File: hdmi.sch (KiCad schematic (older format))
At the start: 31 parts, among them J1901 Mini-HDMI, Q1901 NX3020NAKS, Q1902 NX3020NAKS, Q1903 NX3020NAKS, Q1904 NX3020NAKS, U1901 PCMF3HDMI2SZ, U1902 PCMF2HDMI2SZ

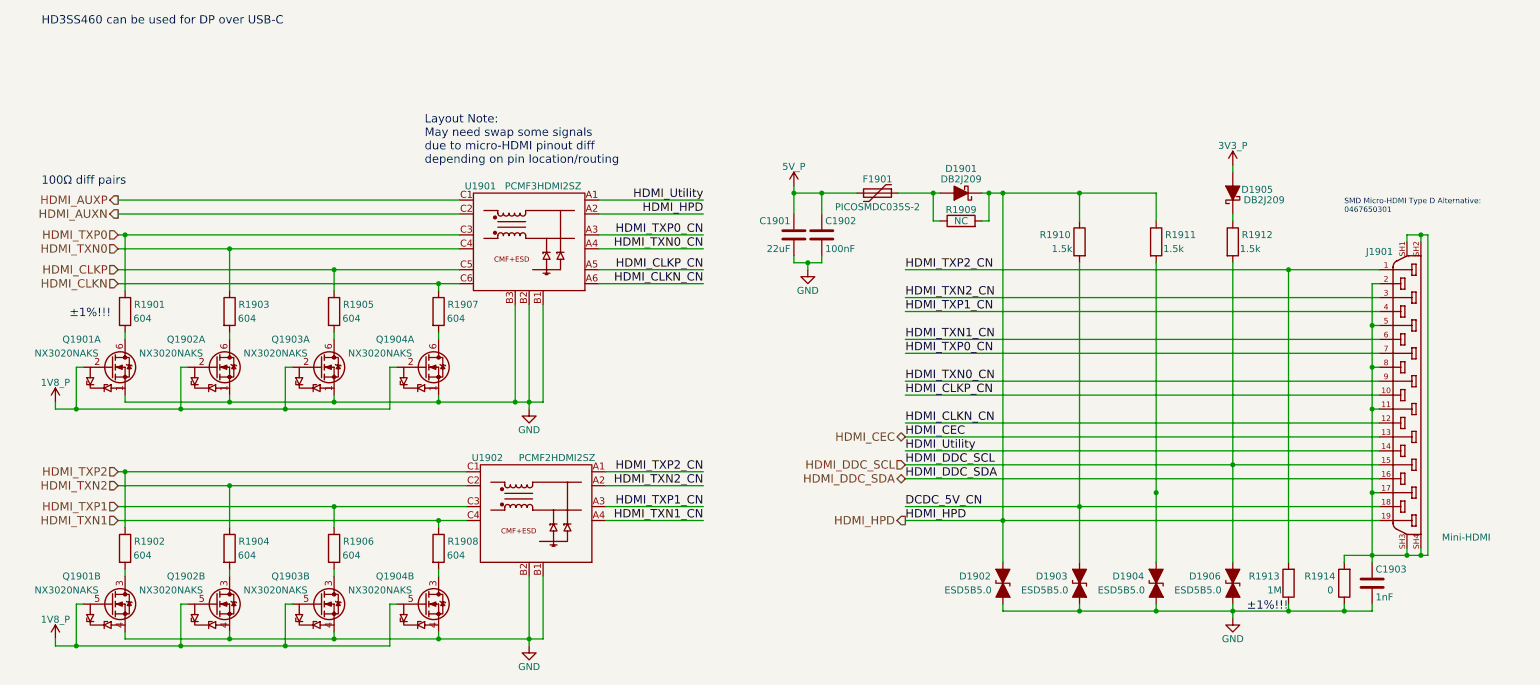
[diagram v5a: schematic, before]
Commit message: Connect VCC of the USB1_VBUS comparitor (TLV3201AIDBVR) to 5V_SOM instead of 5V_P so that VBUS presence can be detected quickly enough for the USB Serial Downloader bootmode, connect the TVS diodes on the HDMI receptacle to the proper pins
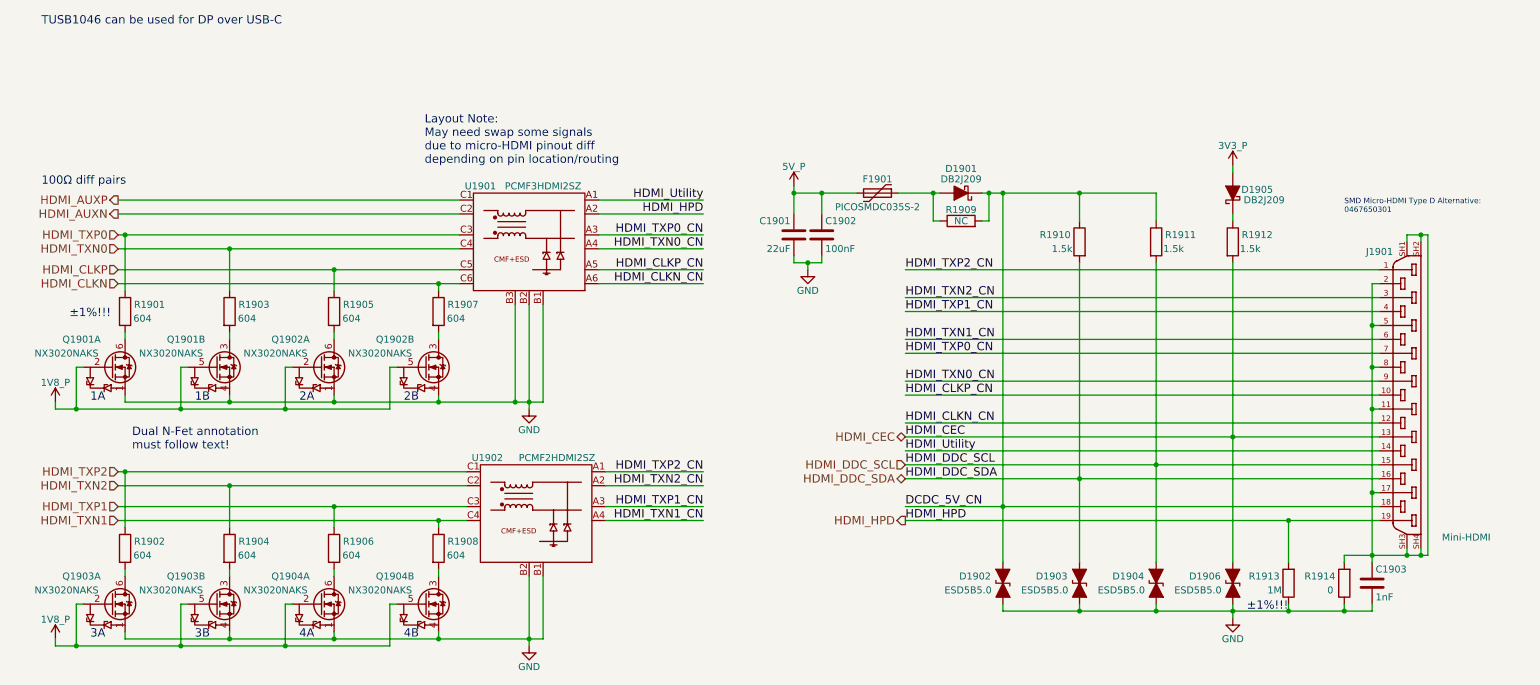
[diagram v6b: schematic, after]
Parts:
- D1902, D1903, D1904, D1906: Distrib PN ESD5B5.0ST1GOSCT-ND -> 10N9401
- F1901: Distrib Link (none) -> https://www.arrow.com/en/products/picosmdc035s-2/littelfuse; Distrib PN (none) -> PICOSMDC035S-2; MFG Name (none) -> Littlefuse; MFG Part Num (none) -> PICOSMDC035S-2; Others (none) -> https://octopart.com/search?q=PICOSMDC035S&start=0; Tolerance (none) -> -
- Q1901, Q1902, Q1903, Q1904: Distrib Link (none) -> https://www.arrow.com/en/products/nx3020naks115/nexperia; Distrib PN (none) -> NX3020NAKS,115; MFG Name (none) -> NXP; MFG Part Num (none) -> NX3020NAKS; Others (none) -> https://octopart.com/search?q=NX3020NAKS&start=0; Tolerance (none) -> -
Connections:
- net DCDC_5V_CN: now also D1901.1 (K), D1902.1 (A1), R1909.2, R1910.1, R1911.1; no longer D1903.1 (A1), R1910.2
- net HDMI_CEC: now also D1906.1 (A1), R1912.2
- net HDMI_DDC_SCL: now also D1904.1 (A1), R1911.2; no longer D1906.1 (A1), R1912.2
- net HDMI_DDC_SDA: now also D1903.1 (A1), R1910.2
- net HDMI_HPD: now also R1913.2; no longer D1901.1 (K), D1902.1 (A1), R1909.2, R1910.1, R1911.1
- net HDMI_TXP2_CN: no longer R1913.2
- net at R1905.2: now also Q1902.6 (D); no longer Q1903.6 (D)
- net at R1903.2: now also Q1901.3 (D); no longer Q1902.6 (D)
- net at R1902.2: now also Q1903.6 (D); no longer Q1901.3 (D)
- net at Q1903.3 (D): now also R1904.2; no longer R1906.2
- net at R1907.2: now also Q1902.3 (D); no longer Q1904.6 (D)
- new net: Q1904.6 (D), R1906.2
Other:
- note added: "1A"
- note added: "1B"
- note added: "2A"
- note added: "2B"
- note added: "3A"
- note added: "3B"
- note added: "4A"
- note added: "4B"
- note added: "Dual N-Fet annotation\nmust follow text!"
- note added: "TUSB1046 can be used for DP over USB-C"
- note removed: "HD3SS460 can be used for DP over USB-C"

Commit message: Add FET (Q* reference designators) footprints
Some footprints are slightly edited versions of their KiCad official library equivalents, using the existing 3D models. DMG2301L's SOT-23 footprint is identical to the official one in the KiCad library.
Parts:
- Q1901, Q1902, Q1903, Q1904: footprint (none) -> dvk-mx8m-bsb:6-TSSOP
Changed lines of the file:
@@
 F 0 "Q1901" H 800 3300 50  0000 L CNN
 F 1 "NX3020NAKS" H 600 3200 50  0000 L CNN
-F 2 "" H 1350 3200 50  0001 C CNN
+F 2 "dvk-mx8m-bsb:6-TSSOP" H 1350 3200 50  0001 C CNN
 F 3 "https://assets.nexperia.com/documents/data-sheet/NX3020NAKS.pdf" H 1150 3100 50  0001 C CNN
 F 4 "NXP" H 1150 3100 60  0001 C CNN "MFG Name"
@@
 F 0 "Q1901" H 1550 3300 50  0000 L CNN
 F 1 "NX3020NAKS" H 1350 3200 50  0000 L CNN
-F 2 "" H 2100 3200 50  0001 C CNN
+F 2 "dvk-mx8m-bsb:6-TSSOP" H 2100 3200 50  0001 C CNN
 F 3 "https://assets.nexperia.com/documents/data-sheet/NX3020NAKS.pdf" H 1900 3100 50  0001 C CNN
 F 4 "NXP" H 1900 3100 60  0001 C CNN "MFG Name"
@@
 F 0 "Q1902" H 2300 3300 50  0000 L CNN
 F 1 "NX3020NAKS" H 2100 3200 50  0000 L CNN
-F 2 "" H 2850 3200 50  0001 C CNN
+F 2 "dvk-mx8m-bsb:6-TSSOP" H 2850 3200 50  0001 C CNN
 F 3 "https://assets.nexperia.com/documents/data-sheet/NX3020NAKS.pdf" H 2650 3100 50  0001 C CNN
 F 4 "NXP" H 2650 3100 60  0001 C CNN "MFG Name"
@@
 F 0 "Q1903" H 800 5000 50  0000 L CNN
 F 1 "NX3020NAKS" H 600 4900 50  0000 L CNN
-F 2 "" H 1350 4900 50  0001 C CNN
+F 2 "dvk-mx8m-bsb:6-TSSOP" H 1350 4900 50  0001 C CNN
 F 3 "https://assets.nexperia.com/documents/data-sheet/NX3020NAKS.pdf" H 1150 4800 50  0001 C CNN
 F 4 "NXP" H 1150 4800 60  0001 C CNN "MFG Name"
@@
 F 0 "Q1904" H 2300 5000 50  0000 L CNN
 F 1 "NX3020NAKS" H 2100 4900 50  0000 L CNN
-F 2 "" H 2850 4900 50  0001 C CNN
+F 2 "dvk-mx8m-bsb:6-TSSOP" H 2850 4900 50  0001 C CNN
 F 3 "https://assets.nexperia.com/documents/data-sheet/NX3020NAKS.pdf" H 2650 4800 50  0001 C CNN
 F 4 "NXP" H 2650 4800 60  0001 C CNN "MFG Name"
@@
 F 0 "Q1902" H 3050 3300 50  0000 L CNN
 F 1 "NX3020NAKS" H 2850 3200 50  0000 L CNN
-F 2 "" H 3600 3200 50  0001 C CNN
+F 2 "dvk-mx8m-bsb:6-TSSOP" H 3600 3200 50  0001 C CNN
 F 3 "https://assets.nexperia.com/documents/data-sheet/NX3020NAKS.pdf" H 3400 3100 50  0001 C CNN
 F 4 "NXP" H 3400 3100 60  0001 C CNN "MFG Name"
@@
 F 0 "Q1903" H 1550 5000 50  0000 L CNN
 F 1 "NX3020NAKS" H 1350 4900 50  0000 L CNN
-F 2 "" H 2100 4900 50  0001 C CNN
+F 2 "dvk-mx8m-bsb:6-TSSOP" H 2100 4900 50  0001 C CNN
 F 3 "https://assets.nexperia.com/documents/data-sheet/NX3020NAKS.pdf" H 1900 4800 50  0001 C CNN
 F 4 "NXP" H 1900 4800 60  0001 C CNN "MFG Name"
@@
 F 0 "Q1904" H 3050 5000 50  0000 L CNN
 F 1 "NX3020NAKS" H 2850 4900 50  0000 L CNN
-F 2 "" H 3600 4900 50  0001 C CNN
+F 2 "dvk-mx8m-bsb:6-TSSOP" H 3600 4900 50  0001 C CNN
 F 3 "https://assets.nexperia.com/documents/data-sheet/NX3020NAKS.pdf" H 3400 4800 50  0001 C CNN
 F 4 "NXP" H 3400 4800 60  0001 C CNN "MFG Name"
